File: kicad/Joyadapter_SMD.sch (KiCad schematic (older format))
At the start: 15 parts, among them J1 AVR-ISP-6, J3 USB_B_Mini, U1 ATtiny4313-SU, X1 DB9_male, X2 DB9_male, Y1 12MHz

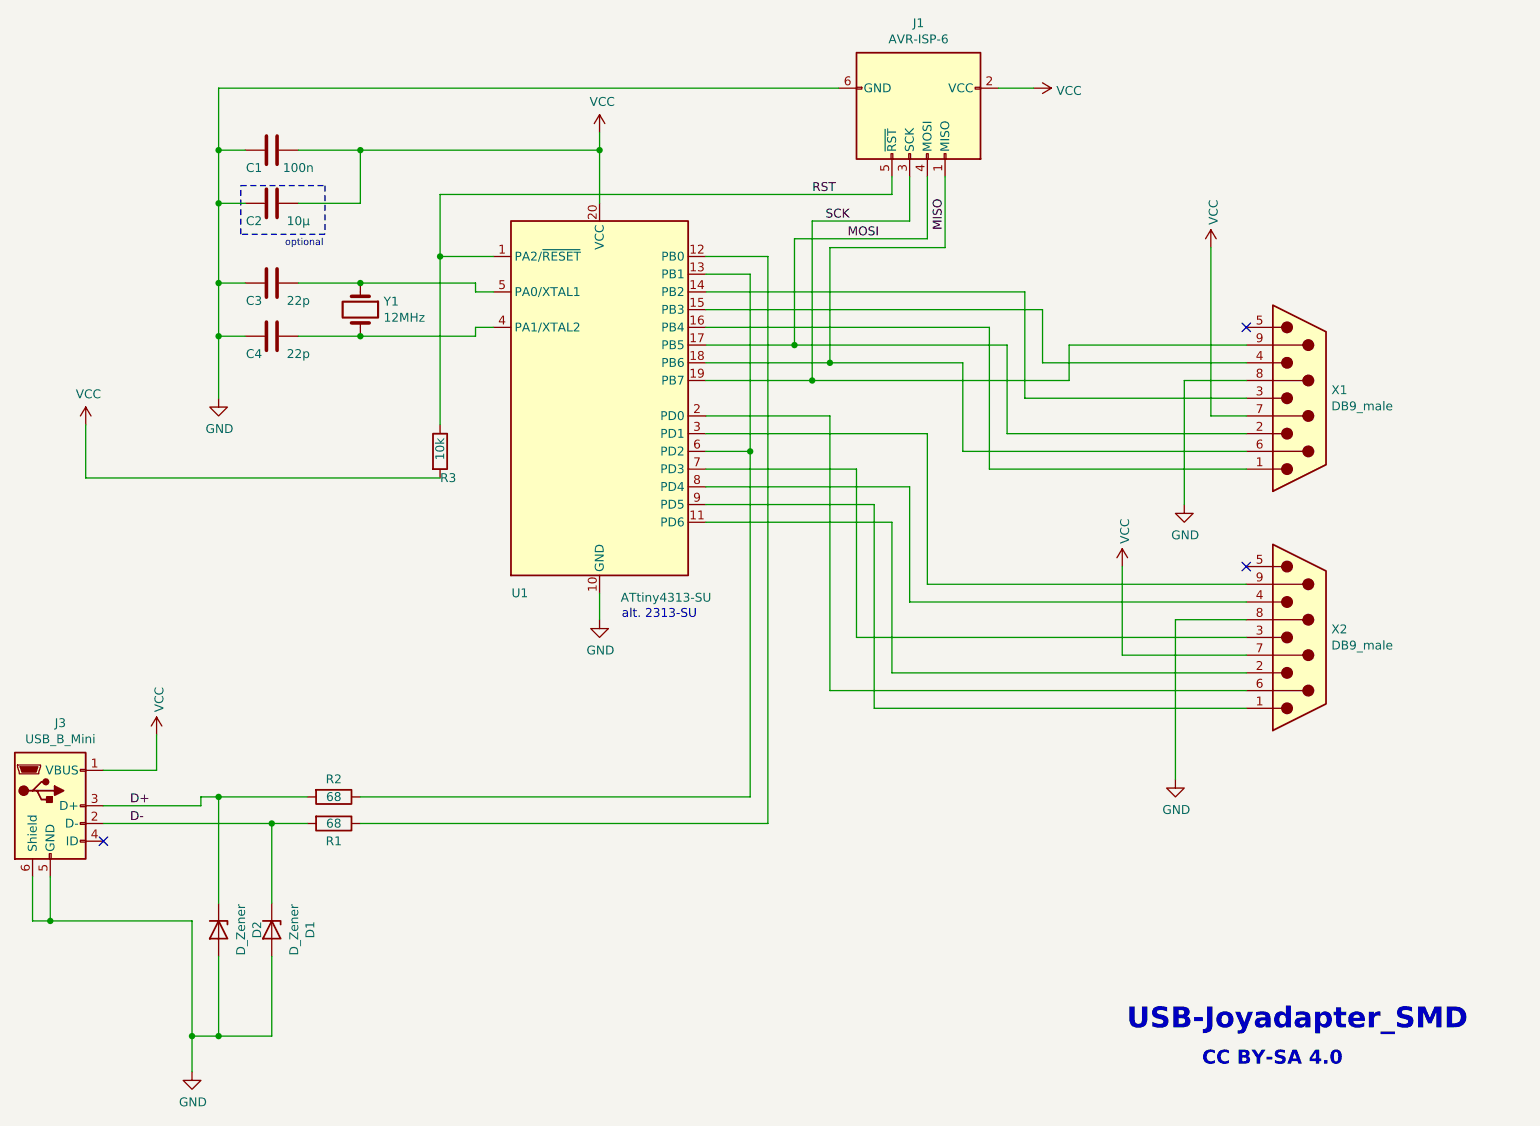
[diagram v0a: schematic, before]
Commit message: Update
Fuse added
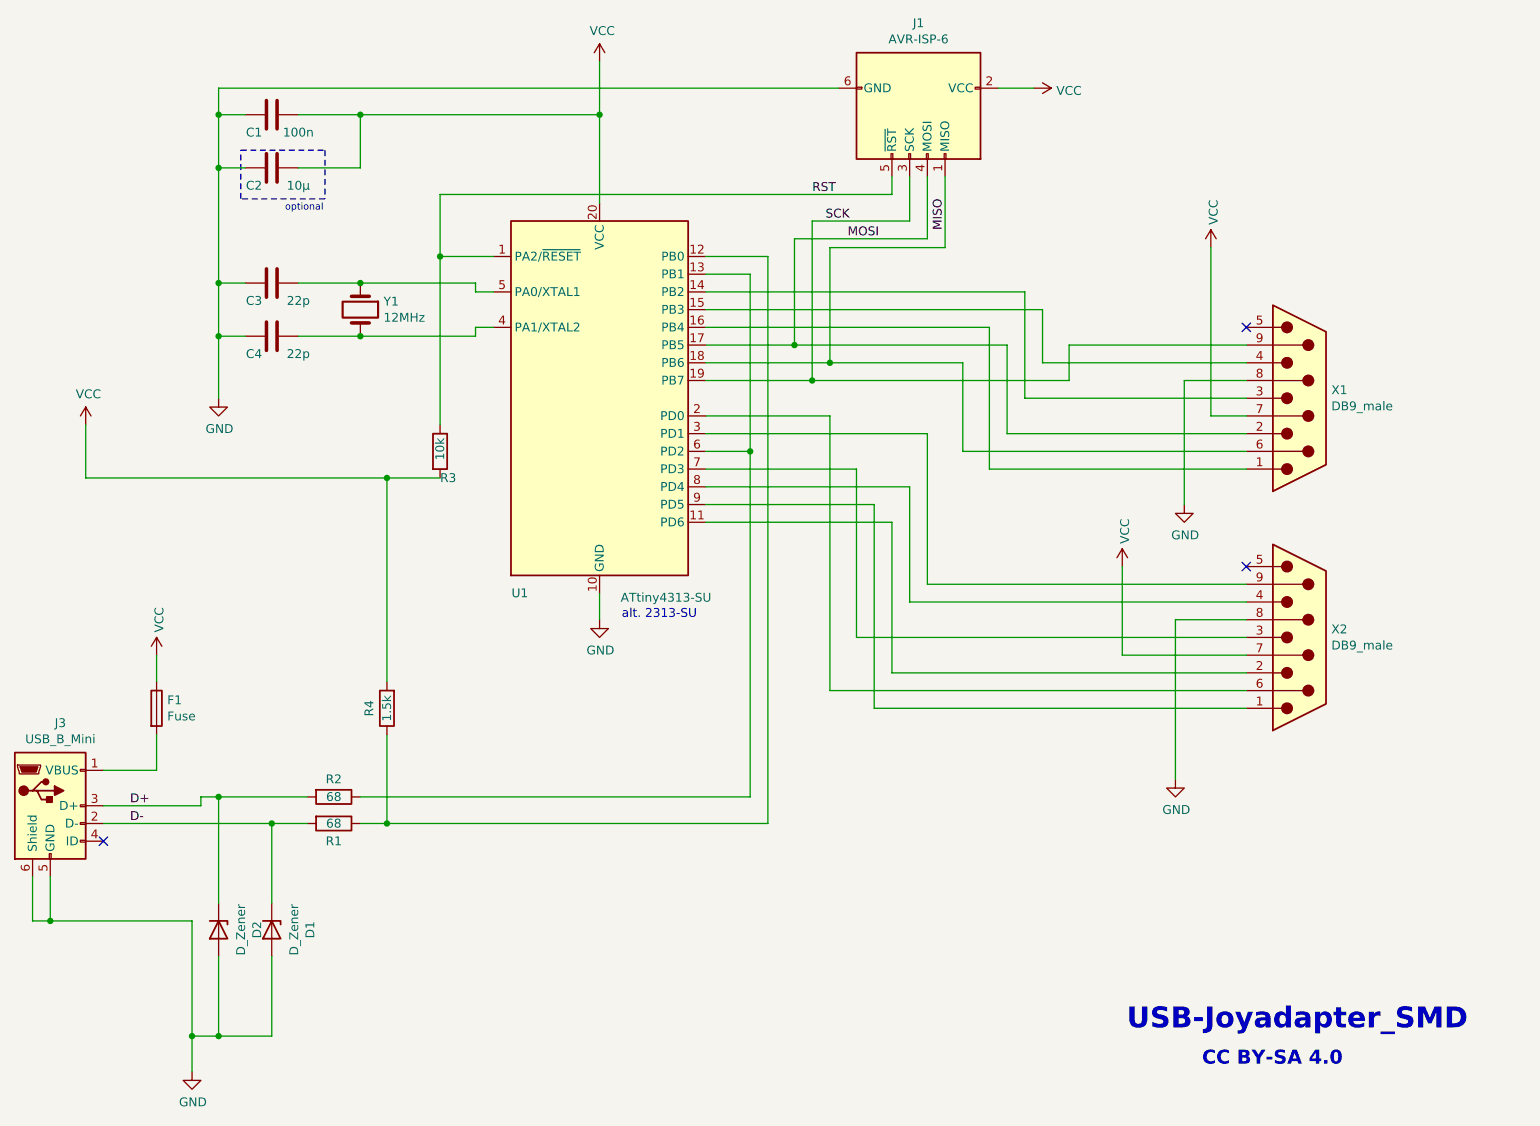
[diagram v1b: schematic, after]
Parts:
- added F1: Fuse, Fuse:Fuse_0805_2012Metric_Pad1.15x1.40mm_HandSolder, symbol Device:Fuse
- added R4: 1.5k, Resistor_SMD:R_0805_2012Metric_Pad1.20x1.40mm_HandSolder, symbol Device:R
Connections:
- net VCC: now also F1.1, R4.2; no longer J3.1 (VBUS)
- net at R1.1, U1.12 (PB0): now also R4.1
- new net: F1.2, J3.1 (VBUS)
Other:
- moved on the sheet: C1, C2
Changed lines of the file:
@@
-$EndComp
-$Comp
-L Connector:AVR-ISP-6 J1
-U 1 1 5FFF709E
-P 6900 1700
-F 0 "J1" V 6433 1750 50  0000 C CNN
-F 1 "AVR-ISP-6" V 6524 1750 50  0000 C CNN
-F 2 "eig_Footprints:PinHeader_1x06_P2.54mm_Vertical" V 6650 1750 50  0001 C CNN
-F 3 " ~" H 5625 1150 50  0001 C CNN
-	1    6900 1700
-	0    1    1    0
 $EndComp
 $Comp
@@
 	4450 2750 4550 2750
 Wire Wire Line
-	6500 1600 3000 1600
-Wire Wire Line
 	3150 3000 3000 3000
 Connection ~ 3000 3000
 Wire Wire Line
 	3000 3000 3000 3350
-Wire Wire Line
-	3150 2700 3000 2700
-Connection ~ 3000 2700
-Wire Wire Line
-	3000 2700 3000 3000
 $Comp
 L Device:C C1
 U 1 1 600012D9
-P 3300 1950
-F 0 "C1" V 3400 1850 50  0000 C CNN
-F 1 "100n" V 3400 2100 50  0000 C CNN
-F 2 "Capacitor_SMD:C_0805_2012Metric_Pad1.18x1.45mm_HandSolder" H 3338 1800 50  0001 C CNN
-F 3 "~" H 3300 1950 50  0001 C CNN
-	1    3300 1950
+P 3300 1750
+F 0 "C1" V 3400 1650 50  0000 C CNN
+F 1 "100n" V 3400 1900 50  0000 C CNN
+F 2 "Capacitor_SMD:C_0805_2012Metric_Pad1.18x1.45mm_HandSolder" H 3338 1600 50  0001 C CNN
+F 3 "~" H 3300 1750 50  0001 C CNN
+	1    3300 1750
 	0    1    1    0
 $EndComp
@@
 	3800 3000 4450 3000
 Wire Wire Line
-	6800 2100 6800 2200
-Wire Wire Line
 	6800 2200 4250 2200
 $Comp
 L power:VCC #PWR0103
 U 1 1 60005873
-P 5150 1850
-F 0 "#PWR0103" H 5150 1700 50  0001 C CNN
-F 1 "VCC" H 5165 2023 50  0000 C CNN
-F 2 "" H 5150 1850 50  0001 C CNN
-F 3 "" H 5150 1850 50  0001 C CNN
-	1    5150 1850
+P 5150 1450
+F 0 "#PWR0103" H 5150 1300 50  0001 C CNN
+F 1 "VCC" H 5165 1623 50  0000 C CNN
+F 2 "" H 5150 1450 50  0001 C CNN
+F 3 "" H 5150 1450 50  0001 C CNN
+	1    5150 1450
 	1    0    0    -1
 $EndComp
@@
 $EndComp
 Wire Wire Line
-	4250 3800 2250 3800
+	4250 3800 3950 3800
 Wire Wire Line
 	2250 3800 2250 3500
@@
 	5150 4600 5150 4450
 Wire Wire Line
-	6900 2100 6900 2350
-Wire Wire Line
 	6900 2350 6350 2350
 Wire Wire Line
@@
 	6350 3250 5750 3250
 Wire Wire Line
-	7100 2100 7100 2500
-Wire Wire Line
 	7100 2500 6450 2500
 Wire Wire Line
@@
 	6450 3150 5750 3150
 Wire Wire Line
-	7000 2100 7000 2450
-Wire Wire Line
 	7000 2450 6250 2450
 Wire Wire Line
@@
 Wire Wire Line
 	6250 3050 5750 3050
-$Comp
-L power:VCC #PWR0105
-U 1 1 6000A809
-P 7600 1600
-F 0 "#PWR0105" H 7600 1450 50  0001 C CNN
-F 1 "VCC" V 7615 1728 50  0000 L CNN
-F 2 "" H 7600 1600 50  0001 C CNN
-F 3 "" H 7600 1600 50  0001 C CNN
-	1    7600 1600
-	0    1    1    0
-$EndComp
-Wire Wire Line
-	7600 1600 7400 1600
 $Comp
 L Joyadapter_SMD-rescue:USB_B_Mini-Connector J3
@@
 	0    1    1    0
 $EndComp
-Wire Wire Line
-	3000 1600 3000 1950
 $Comp
 L Device:C C2
 U 1 1 60078C62
-P 3300 2250
-F 0 "C2" V 3400 2150 50  0000 C CNN
-F 1 "10µ" V 3400 2400 50  0000 C CNN
-F 2 "Capacitor_Tantalum_SMD:CP_EIA-3216-18_Kemet-A_Pad1.58x1.35mm_HandSolder" H 3338 2100 50  0001 C CNN
-F 3 "~" H 3300 2250 50  0001 C CNN
-	1    3300 2250
-	0    1    1    0
-$EndComp
-Wire Wire Line
-	3150 2250 3000 2250
-Connection ~ 3000 2250
-Wire Wire Line
-	3000 2250 3000 2700
-Wire Wire Line
-	3150 1950 3000 1950
-Connection ~ 3000 1950
-Wire Wire Line
-	3000 1950 3000 2250
-Wire Wire Line
-	5150 1850 5150 1950
-Wire Wire Line
-	3450 1950 3800 1950
-Connection ~ 5150 1950
-Wire Wire Line
-	5150 1950 5150 2250
-Wire Wire Line
-	3450 2250 3800 2250
-Wire Wire Line
-	3800 2250 3800 1950
-Connection ~ 3800 1950
-Wire Wire Line
-	3800 1950 5150 1950
+P 3300 2050
+F 0 "C2" V 3400 1950 50  0000 C CNN
+F 1 "10µ" V 3400 2200 50  0000 C CNN
+F 2 "Capacitor_Tantalum_SMD:CP_EIA-3216-18_Kemet-A_Pad1.58x1.35mm_HandSolder" H 3338 1900 50  0001 C CNN
+F 3 "~" H 3300 2050 50  0001 C CNN
+	1    3300 2050
+	0    1    1    0
+$EndComp
+Wire Wire Line
+	3150 2050 3000 2050
+Connection ~ 3000 2050
+Wire Wire Line
+	3150 1750 3000 1750
+Connection ~ 3000 1750
+Wire Wire Line
+	3000 1750 3000 2050
+Wire Wire Line
+	3450 1750 3800 1750
+Wire Wire Line
+	3450 2050 3800 2050
+Wire Wire Line
+	3800 2050 3800 1750
+Connection ~ 3800 1750
+Wire Wire Line
+	3800 1750 5150 1750
 Wire Wire Line
 	5750 2950 7350 2950
@@
 L power:VCC #PWR0109
 U 1 1 600A2F8B
-P 2650 5250
-F 0 "#PWR0109" H 2650 5100 50  0001 C CNN
-F 1 "VCC" V 2665 5378 50  0000 L CNN
-F 2 "" H 2650 5250 50  0001 C CNN
-F 3 "" H 2650 5250 50  0001 C CNN
-	1    2650 5250
+P 2650 4800
+F 0 "#PWR0109" H 2650 4650 50  0001 C CNN
+F 1 "VCC" V 2665 4928 50  0000 L CNN
+F 2 "" H 2650 4800 50  0001 C CNN
+F 3 "" H 2650 4800 50  0001 C CNN
+	1    2650 4800
 	1    0    0    -1
 $EndComp
@@
 	6100 2550 6100 5750
 Wire Wire Line
-	6100 5750 3800 5750
+	6100 5750 3950 5750
 Wire Wire Line
 	5750 2650 6000 2650
@@
 NoConn ~ 8800 4300
 Wire Notes Line
-	3125 2150 3600 2150
+	3125 1950 3600 1950
 Wire Notes Line
-	3600 2150 3600 2425
+	3600 1950 3600 2225
 Wire Notes Line
-	3600 2425 3125 2425
+	3600 2225 3125 2225
 Wire Notes Line
-	3125 2425 3125 2150
-Text Notes 3375 2500 0    39   ~ 0
+	3125 2225 3125 1950
+Text Notes 3375 2300 0    39   ~ 0
 optional
 Wire Wire Line
@@
 Wire Wire Line
 	2850 7150 2850 6950
+$Comp
+L Device:R R4
+U 1 1 6009C109
+P 3950 5100
+F 0 "R4" V 4050 5100 50  0000 C CNN
+F 1 "1.5k" V 3950 5100 50  0000 C CNN
+F 2 "Resistor_SMD:R_0805_2012Metric_Pad1.20x1.40mm_HandSolder" V 3880 5100 50  0001 C CNN
+F 3 "~" H 3950 5100 50  0001 C CNN
+	1    3950 5100
+	-1   0    0    1
+$EndComp
+Wire Wire Line
+	3150 2700 3000 2700
+Connection ~ 3000 2700
+Wire Wire Line
+	3000 2700 3000 3000
+Wire Wire Line
+	5150 1450 5150 1750
+Connection ~ 5150 1750
+Wire Wire Line
+	5150 1750 5150 2250
+Wire Wire Line
+	3000 2050 3000 2700
+Wire Wire Line
+	7100 2100 7100 2500
+Wire Wire Line
+	7000 2100 7000 2450
+Wire Wire Line
+	6900 2100 6900 2350
+Wire Wire Line
+	6800 2100 6800 2200
+Wire Wire Line
+	3000 1600 3000 1750
+Wire Wire Line
+	6500 1600 3000 1600
+Wire Wire Line
+	7600 1600 7400 1600
+$Comp
+L power:VCC #PWR0105
+U 1 1 6000A809
+P 7600 1600
+F 0 "#PWR0105" H 7600 1450 50  0001 C CNN
+F 1 "VCC" V 7615 1728 50  0000 L CNN
+F 2 "" H 7600 1600 50  0001 C CNN
+F 3 "" H 7600 1600 50  0001 C CNN
+	1    7600 1600
+	0    1    1    0
+$EndComp
+$Comp
+L Connector:AVR-ISP-6 J1
+U 1 1 5FFF709E
+P 6900 1700
+F 0 "J1" V 6433 1750 50  0000 C CNN
+F 1 "AVR-ISP-6" V 6524 1750 50  0000 C CNN
+F 2 "eig_Footprints:PinHeader_1x06_P2.54mm_Vertical" V 6650 1750 50  0001 C CNN
+F 3 " ~" H 5625 1150 50  0001 C CNN
+	1    6900 1700
+	0    1    1    0
+$EndComp
+Wire Wire Line
+	3950 5250 3950 5750
+Connection ~ 3950 5750
+Wire Wire Line
+	3950 5750 3800 5750
+Wire Wire Line
+	3950 4950 3950 3800
+Connection ~ 3950 3800
+Wire Wire Line
+	3950 3800 2250 3800
+$Comp
+L Device:Fuse F1
+U 1 1 600E9265
+P 2650 5100
+F 0 "F1" H 2710 5146 50  0000 L CNN
+F 1 "Fuse" H 2710 5055 50  0000 L CNN
+F 2 "Fuse:Fuse_0805_2012Metric_Pad1.15x1.40mm_HandSolder" V 2580 5100 50  0001 C CNN
+F 3 "~" H 2650 5100 50  0001 C CNN
+	1    2650 5100
+	1    0    0    -1
+$EndComp
+Wire Wire Line
+	2650 4950 2650 4800
 $EndSCHEMATC
